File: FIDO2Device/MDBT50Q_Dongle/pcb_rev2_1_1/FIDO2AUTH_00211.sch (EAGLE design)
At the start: 36 parts, among them CN1 TE-1734028, CN2 IF_4PIN, CN3 IF_2PIN_SOL, CN5 IF_2PIN_SOL, SW1 SKRPACE010, SW2 SKTADAE010, U1 MDBT50Q-P1M, U2 XC6206P332MR-G, X1 NX3215SA-32.768K

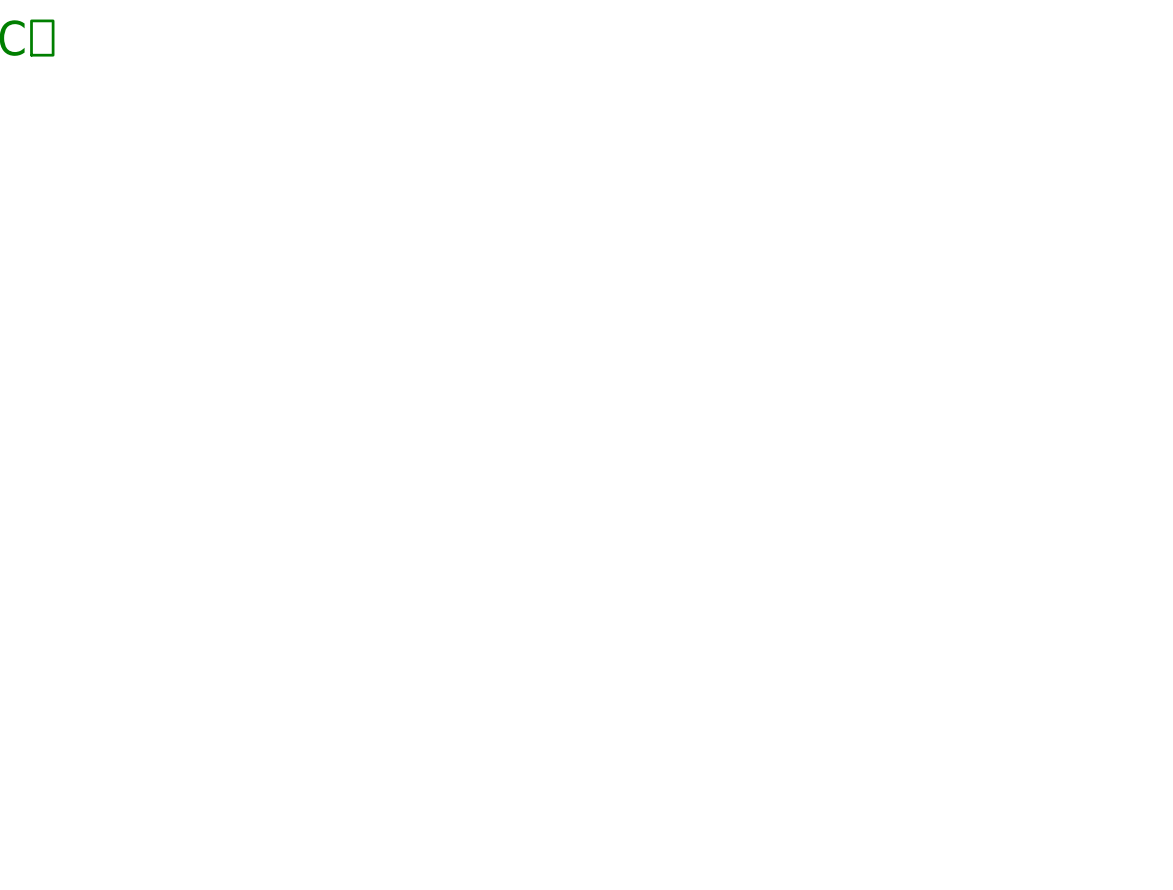
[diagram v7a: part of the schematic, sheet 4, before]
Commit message: 回路図を修正
・セキュアIC関連部品を追加
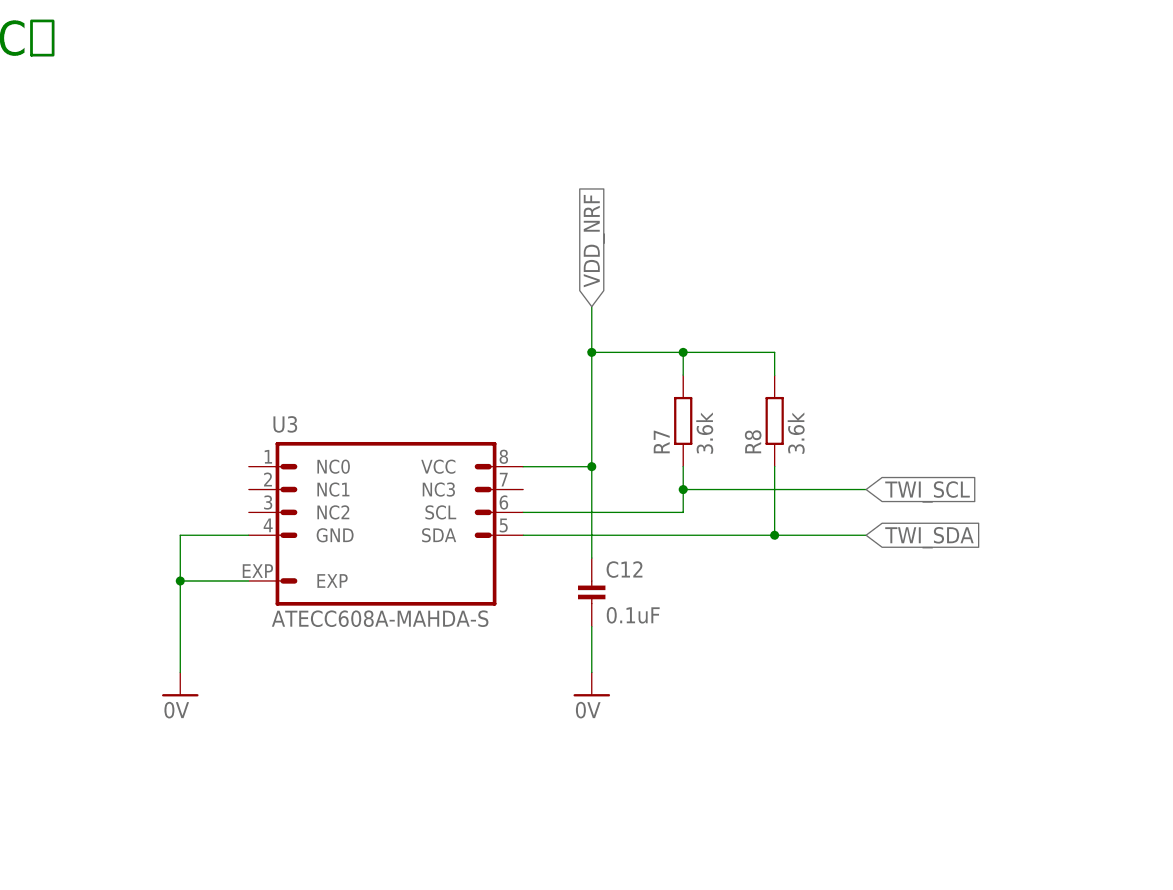
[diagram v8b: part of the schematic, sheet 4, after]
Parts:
- added C12: 0.1uF, Parts:CAP_0402
- added R7, R8: 3.6k, Parts:RESISTOR_0402
- added U3: ATECC608A-MAHDA-S, ICs:ATECC608A-MAHDA-S
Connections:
- net 0V: now also C12.2, U3.EXP, U3.GND
- net TWI_SCL: now also R7.1, U3.SCL
- net TWI_SDA: now also R8.1, U3.SDA
- net VDD_NRF: now also C12.1, R7.2, R8.2, U3.VCC
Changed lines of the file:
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@@
 <part name="CN5" library="Connectors" deviceset="IF_2PIN" device="_SOL" value="IF_2PIN_SOL"/>
 <part name="CN3" library="Connectors" deviceset="IF_2PIN" device="_SOL"/>
+<part name="U3" library="ICs" deviceset="ATECC608A" device="-MAHDA-S"/>
+<part name="GND19" library="Supply" deviceset="0V" device=""/>
+<part name="C12" library="Parts" deviceset="CAP" device="_0402" value="0.1uF"/>
+<part name="GND20" library="Supply" deviceset="0V" device=""/>
+<part name="R7" library="Parts" deviceset="RESISTOR" device="_0402" value="3.6k"/>
+<part name="R8" library="Parts" deviceset="RESISTOR" device="_0402" value="3.6k"/>
 </parts>
 <sheets>
@@
 <instances>
 <instance part="FRAME4" gate="G$1" x="0" y="0"/>
+<instance part="U3" gate="G$1" x="99.06" y="93.98"/>
+<instance part="GND19" gate="1" x="91.44" y="71.12"/>
+<instance part="C12" gate="G$1" x="137.16" y="86.36"/>
+<instance part="GND20" gate="1" x="137.16" y="71.12"/>
+<instance part="R7" gate="G$1" x="147.32" y="96.52" rot="R90"/>
+<instance part="R8" gate="G$1" x="157.48" y="96.52" rot="R90"/>
 </instances>
 <busses>
 </busses>
 <nets>
+<net name="0V" class="0">
+<segment>
+<pinref part="U3" gate="G$1" pin="EXP"/>
+<pinref part="GND19" gate="1" pin="0V"/>
+<wire x1="99.06" y1="83.82" x2="91.44" y2="83.82" width="0.1524" layer="91"/>
+<wire x1="91.44" y1="83.82" x2="91.44" y2="73.66" width="0.1524" layer="91"/>
+<pinref part="U3" gate="G$1" pin="GND"/>
+<wire x1="99.06" y1="88.9" x2="91.44" y2="88.9" width="0.1524" layer="91"/>
+<wire x1="91.44" y1="88.9" x2="91.44" y2="83.82" width="0.1524" layer="91"/>
+<junction x="91.44" y="83.82"/>
+</segment>
+<segment>
+<pinref part="GND20" gate="1" pin="0V"/>
+<pinref part="C12" gate="G$1" pin="2"/>
+<wire x1="137.16" y1="73.66" x2="137.16" y2="78.74" width="0.1524" layer="91"/>
+</segment>
+</net>
+<net name="VDD_NRF" class="0">
+<segment>
+<pinref part="U3" gate="G$1" pin="VCC"/>
+<pinref part="C12" gate="G$1" pin="1"/>
+<wire x1="129.54" y1="96.52" x2="137.16" y2="96.52" width="0.1524" layer="91"/>
+<wire x1="137.16" y1="96.52" x2="137.16" y2="86.36" width="0.1524" layer="91"/>
+<pinref part="R7" gate="G$1" pin="2"/>
+<wire x1="147.32" y1="106.68" x2="147.32" y2="109.22" width="0.1524" layer="91"/>
+<wire x1="147.32" y1="109.22" x2="137.16" y2="109.22" width="0.1524" layer="91"/>
+<wire x1="137.16" y1="109.22" x2="137.16" y2="96.52" width="0.1524" layer="91"/>
+<junction x="137.16" y="96.52"/>
+<pinref part="R8" gate="G$1" pin="2"/>
+<wire x1="157.48" y1="106.68" x2="157.48" y2="109.22" width="0.1524" layer="91"/>
+<wire x1="157.48" y1="109.22" x2="147.32" y2="109.22" width="0.1524" layer="91"/>
+<junction x="147.32" y="109.22"/>
+<wire x1="137.16" y1="109.22" x2="137.16" y2="114.3" width="0.1524" layer="91"/>
+<junction x="137.16" y="109.22"/>
+<label x="137.16" y="114.3" size="1.778" layer="95" rot="R90" xref="yes"/>
+</segment>
+</net>
+<net name="TWI_SCL" class="0">
+<segment>
+<pinref part="U3" gate="G$1" pin="SCL"/>
+<pinref part="R7" gate="G$1" pin="1"/>
+<wire x1="129.54" y1="91.44" x2="147.32" y2="91.44" width="0.1524" layer="91"/>
+<wire x1="147.32" y1="91.44" x2="147.32" y2="93.98" width="0.1524" layer="91"/>
+<wire x1="147.32" y1="93.98" x2="147.32" y2="96.52" width="0.1524" layer="91"/>
+<wire x1="147.32" y1="93.98" x2="167.64" y2="93.98" width="0.1524" layer="91"/>
+<junction x="147.32" y="93.98"/>
+<label x="167.64" y="93.98" size="1.778" layer="95" xref="yes"/>
+</segment>
+</net>
+<net name="TWI_SDA" class="0">
+<segment>
+<pinref part="U3" gate="G$1" pin="SDA"/>
+<pinref part="R8" gate="G$1" pin="1"/>
+<wire x1="129.54" y1="88.9" x2="157.48" y2="88.9" width="0.1524" layer="91"/>
+<wire x1="157.48" y1="88.9" x2="157.48" y2="96.52" width="0.1524" layer="91"/>
+<junction x="157.48" y="88.9"/>
+<wire x1="157.48" y1="88.9" x2="167.64" y2="88.9" width="0.1524" layer="91"/>
+<label x="167.64" y="88.9" size="1.778" layer="95" xref="yes"/>
+</segment>
+</net>
 </nets>
 </sheet>
